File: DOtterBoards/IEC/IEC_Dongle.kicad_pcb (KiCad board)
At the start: 2 copper layers, 40 x 47 mm, 14 parts, among them J1 SDF-60J, J2 IDC_2x03

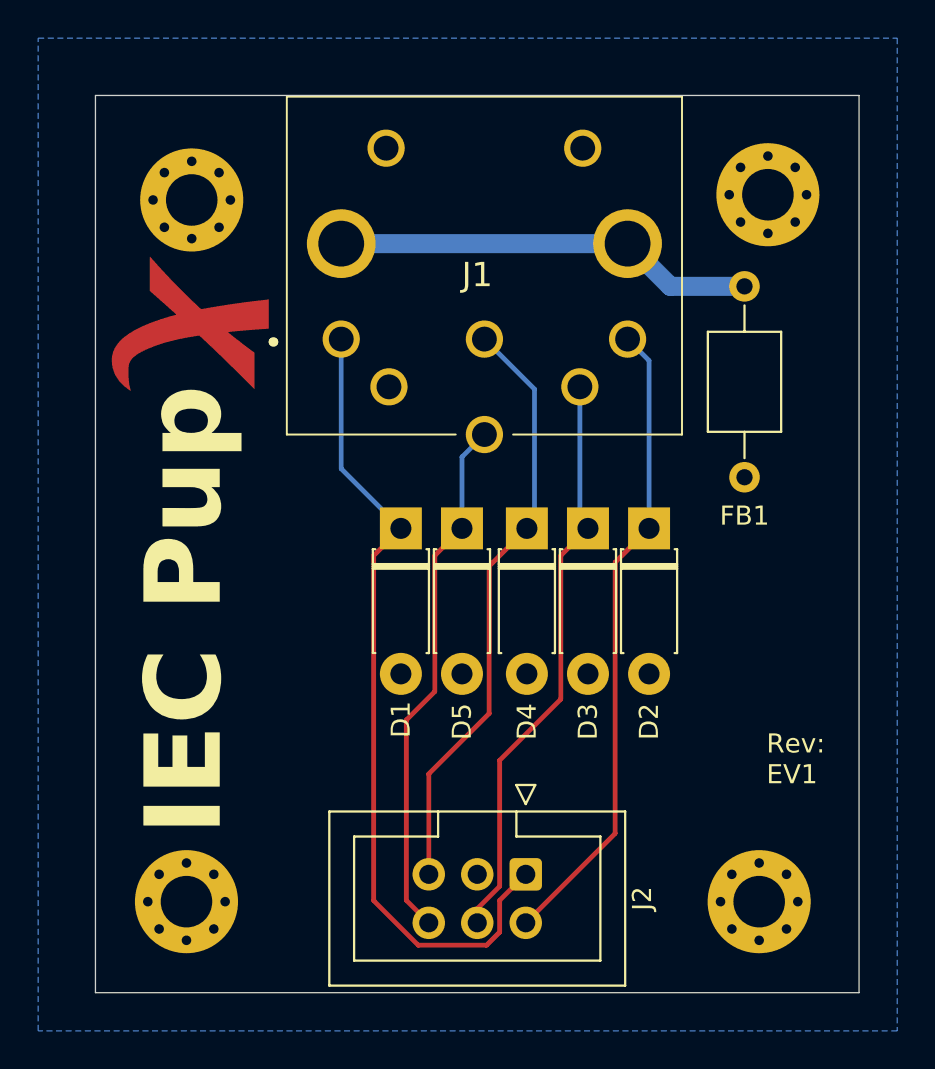
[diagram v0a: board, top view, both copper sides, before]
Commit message: Rename dongle boards to D'Otterboards
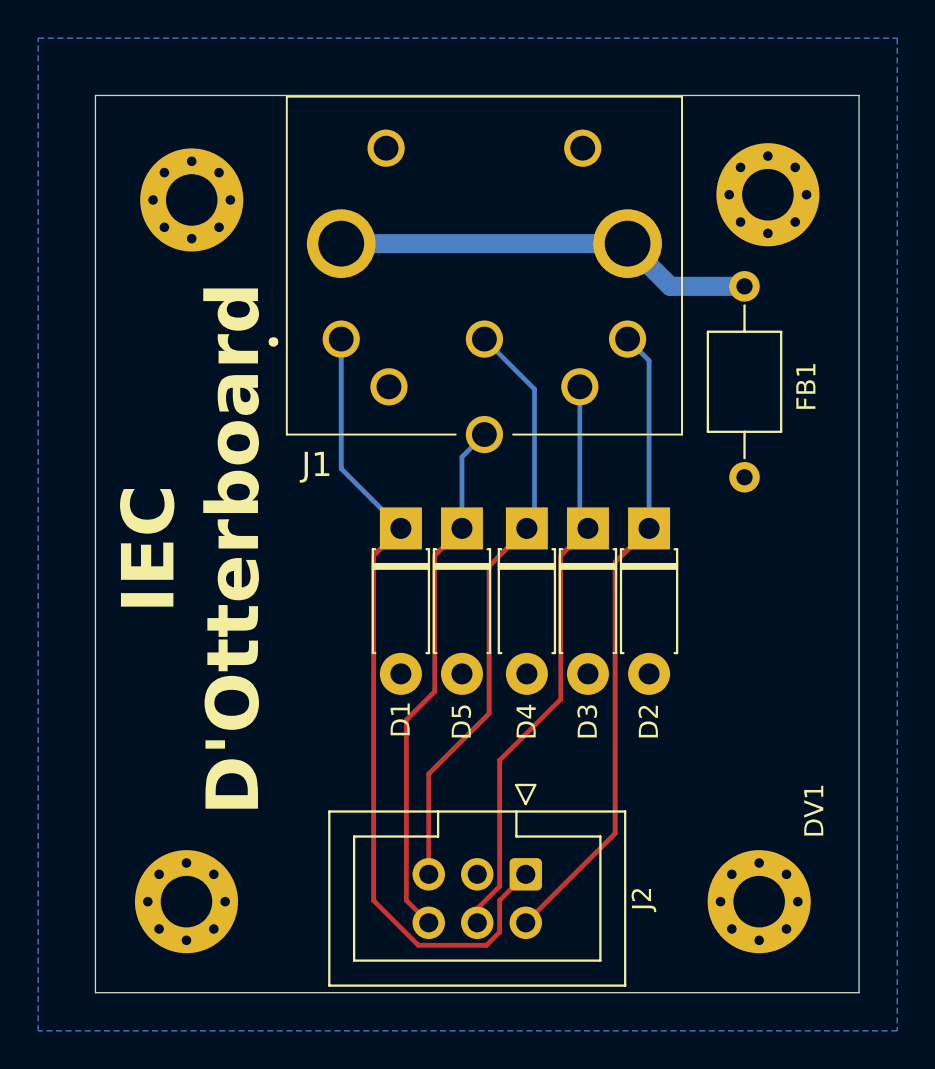
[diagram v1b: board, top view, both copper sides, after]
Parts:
- removed G***: LOGO, OtterX:Fancy_X_FCu
- removed G***: LOGO, OtterX:Fancy_X_Mask
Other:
- board text added: "DV1"
- board text added: "IEC D'Otterboard"
- board text removed: "IEC Pup"
- board text removed: "Rev: EV1"
